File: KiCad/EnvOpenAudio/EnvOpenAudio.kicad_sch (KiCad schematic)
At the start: 76 parts, among them J1 USB_C_Receptacle_USB2.0, J2 SM03B-SRSS-TB, J3 Conn_01x10, SW1 B3U-1000, SW2 B3U-1000, U1 W25Q16JVUXIQ, U2 TPS63001DRCR, U3 TLV75518PDBV, U4 RP2350_60QFN, U5 TLV320AIC3100, U6 LM3880, Y1 ABM8-272-T3

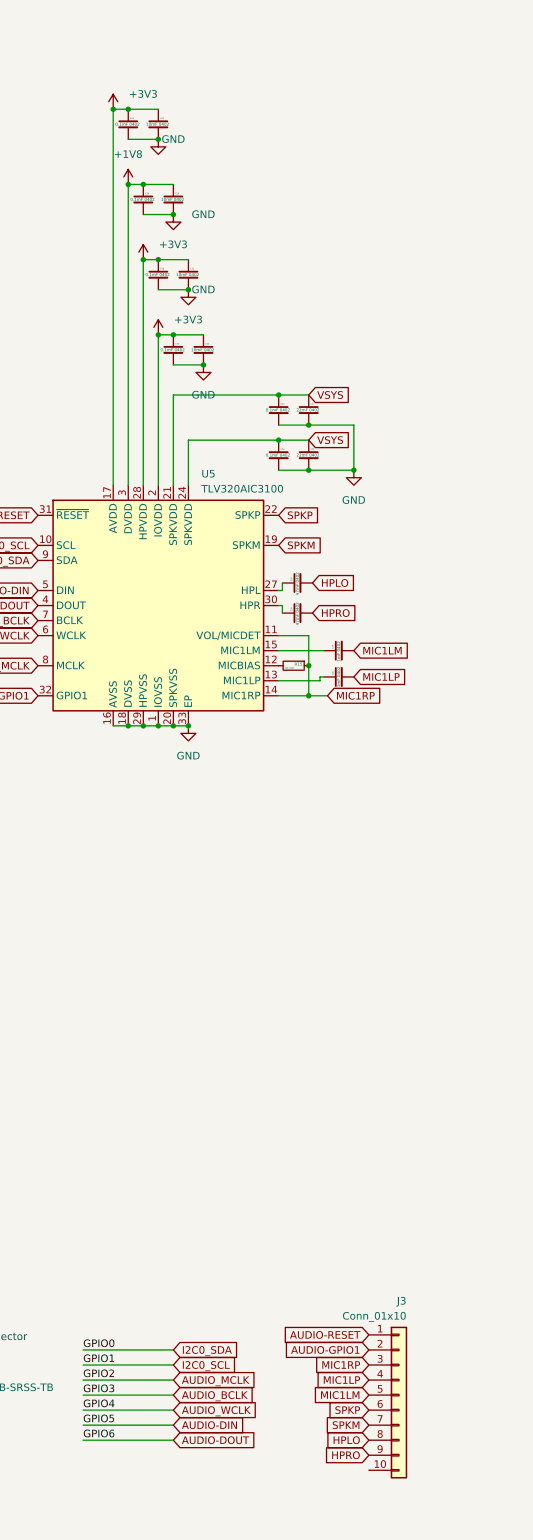
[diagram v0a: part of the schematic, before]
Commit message: changed some component sizes, values ,added seperate analogue ground with small stitching to digital ground.
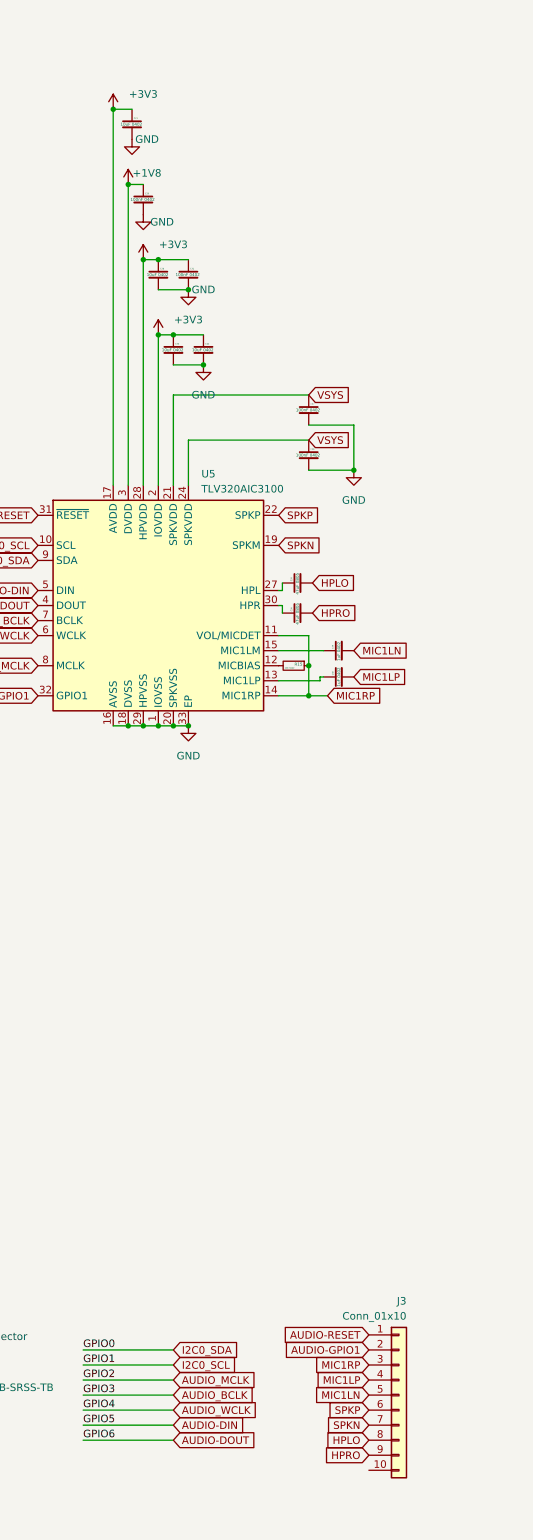
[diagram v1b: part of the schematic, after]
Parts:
- removed C25, C26, C33, C34: 0.1mF 0402, Capacitor_SMD:C_0402_1005Metric, symbol Device:C_Small
- C27, C32: value 10mF 0402 -> 10uF 0402
- C28, C30: value 0.1mF 0402 -> 10uF 0402
- C29, C31: value 10mF 0402 -> 100nF 0402
- C35, C36: value 47mF 0402 -> 47uF 0805; footprint Capacitor_SMD:C_0402_1005Metric -> Capacitor_SMD:C_0805_2012Metric
- C37, C38: value 22mF 0402 -> 100nF 0402
- C39, C40: value 1mF 0402 -> 1uF 0402
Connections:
- net MIC1LM renamed MIC1LN
- net SPKM renamed SPKN
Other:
- moved on the sheet: C27, C29
